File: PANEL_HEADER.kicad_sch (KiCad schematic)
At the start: 1 part, among them J4 Conn_01x02

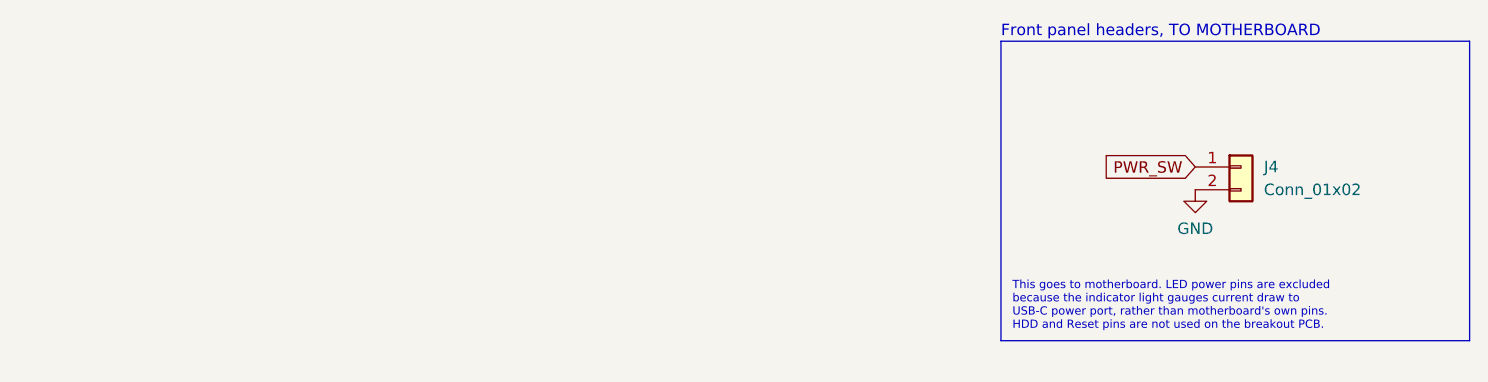
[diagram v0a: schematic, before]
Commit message: Mostly complete initial transfer to hierarchical schematic
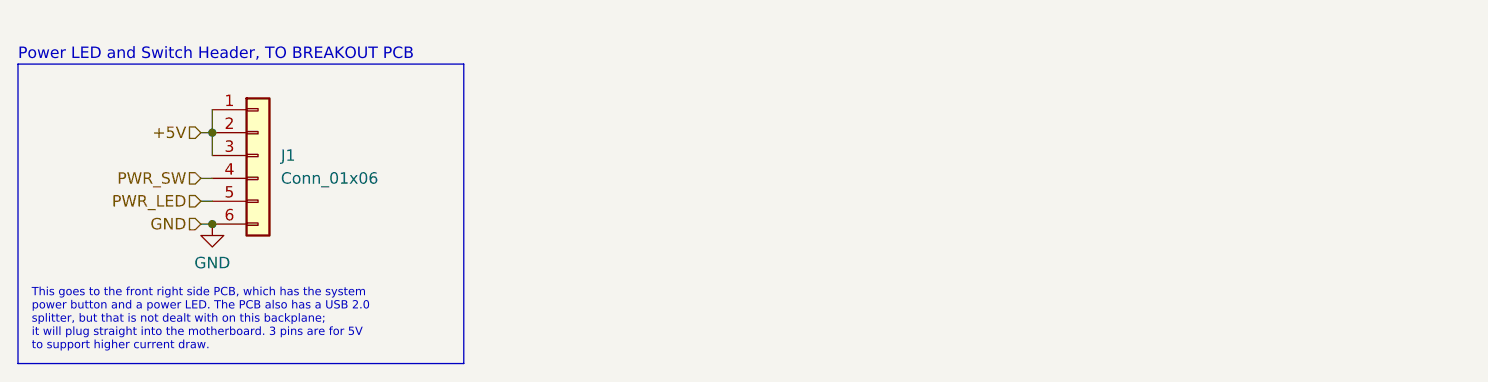
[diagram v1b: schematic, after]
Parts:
- removed J4: Conn_01x02, Connector_PinHeader_2.54mm:PinHeader_1x02_P2.54mm_Vertical_SMD_Pin1Left, symbol Connector_Generic:Conn_01x02
- added J1: Conn_01x06, Connector_PinSocket_2.54mm:PinSocket_1x06_P2.54mm_Horizontal, symbol Connector_Generic:Conn_01x06
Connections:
- net GND: now also J1.6 (Pin_6)
- net PWR_SW: now also J1.4 (Pin_4)
- new net +5V: J1.1 (Pin_1), J1.2 (Pin_2), J1.3 (Pin_3)
- new net PWR_LED: J1.5 (Pin_5)
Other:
- note added: "Power LED and Switch Header, TO BREAKOUT PCB"
- note added: "This goes to the front right side PCB, which has the system power button and a power LED. The PCB also has a USB 2.0 splitter, but that is not dealt with on this backplane; it will plug straight into the motherboard. 3 pins are for 5V to support higher current draw."
- note removed: "Front panel headers, TO MOTHERBOARD"
- note removed: "This goes to motherboard. LED power pins are excluded because the indicator light gauges current draw to USB-C power port, rather than motherboard's own pins. HDD and Reset pins are not used on the breakout PCB."
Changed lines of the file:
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@@
 	(paper "A5")
 	(rectangle
-		(start 133.35 20.32)
-		(end 185.42 53.594)
+		(start 24.13 22.86)
+		(end 73.66 56.134)
 		(stroke
 			(width 0)
@@
 		)
 	)
-	(text "Front panel headers, TO MOTHERBOARD"
-		(exclude_from_sim no)
-		(at 133.35 19.304 0)
-		(effects
-			(font
-				(size 1.27 1.27)
+	(text "This goes to the front right side PCB, which has the system \npower button and a power LED. The PCB also has a USB 2.0\nsplitter, but that is not dealt with on this backplane;\nit will plug straight into the motherboard. 3 pins are for 5V\nto support higher current draw."
+		(exclude_from_sim no)
+		(at 25.654 51.308 0)
+		(effects
+			(font
+				(size 0.9144 0.9144)
 			)
 			(justify left)
 		)
 	)
-	(text "This goes to motherboard. LED power pins are excluded\nbecause the indicator light gauges current draw to\nUSB-C power port, rather than motherboard's own pins.\nHDD and Reset pins are not used on the breakout PCB."
-		(exclude_from_sim no)
-		(at 134.62 49.784 0)
-		(effects
-			(font
-				(size 0.9144 0.9144)
+	(text "Power LED and Switch Header, TO BREAKOUT PCB"
+		(exclude_from_sim no)
+		(at 24.13 21.844 0)
+		(effects
+			(font
+				(size 1.27 1.27)
 			)
 			(justify left)
 		)
 	)
-	(global_label "PWR_SW"
-		(shape input)
-		(at 154.94 34.29 180)
-		(fields_autoplaced yes)
-		(effects
-			(font
-				(size 1.27 1.27)
-			)
-			(justify right)
-		)
-		(property "Intersheetrefs" "${INTERSHEET_REFS}"
-			(at 144.3349 34.29 0)
-			(hide yes)
-			(show_name no)
-			(do_not_autoplace no)
-			(effects
-				(font
-					(size 1.27 1.27)
-				)
-				(justify right)
-			)
+	(junction
+		(at 45.72 30.48)
+		(diameter 0)
+		(color 0 0 0 0)
+	)
+	(junction
+		(at 45.72 40.64)
+		(diameter 0)
+		(color 0 0 0 0)
+	)
+	(wire
+		(pts
+			(xy 44.45 35.56) (xy 45.72 35.56)
+		)
+		(stroke
+			(width 0)
+			(type default)
+		)
+	)
+	(wire
+		(pts
+			(xy 44.45 38.1) (xy 45.72 38.1)
+		)
+		(stroke
+			(width 0)
+			(type default)
+		)
+	)
+	(wire
+		(pts
+			(xy 45.72 27.94) (xy 45.72 30.48)
+		)
+		(stroke
+			(width 0)
+			(type default)
+		)
+	)
+	(wire
+		(pts
+			(xy 44.45 40.64) (xy 45.72 40.64)
+		)
+		(stroke
+			(width 0)
+			(type default)
+		)
+	)
+	(wire
+		(pts
+			(xy 45.72 30.48) (xy 45.72 33.02)
+		)
+		(stroke
+			(width 0)
+			(type default)
+		)
+	)
+	(wire
+		(pts
+			(xy 44.45 30.48) (xy 45.72 30.48)
+		)
+		(stroke
+			(width 0)
+			(type default)
+		)
+	)
+	(hierarchical_label "GND"
+		(shape input)
+		(at 44.45 40.64 180)
+		(effects
+			(font
+				(size 1.27 1.27)
+			)
+			(justify right)
+		)
+	)
+	(hierarchical_label "PWR_SW"
+		(shape input)
+		(at 44.45 35.56 180)
+		(effects
+			(font
+				(size 1.27 1.27)
+			)
+			(justify right)
+		)
+	)
+	(hierarchical_label "+5V"
+		(shape input)
+		(at 44.45 30.48 180)
+		(effects
+			(font
+				(size 1.27 1.27)
+			)
+			(justify right)
+		)
+	)
+	(hierarchical_label "PWR_LED"
+		(shape input)
+		(at 44.45 38.1 180)
+		(effects
+			(font
+				(size 1.27 1.27)
+			)
+			(justify right)
 		)
 	)
 	(symbol
-		(lib_id "power:GND")
-		(at 154.94 36.83 0)
-		(unit 1)
-		(body_style 1)
-		(exclude_from_sim no)
-		(in_bom yes)
-		(on_board yes)
-		(in_pos_files yes)
-		(dnp no)
-		(property "Reference" "#PWR0143"
-			(at 154.94 43.18 0)
-			(hide yes)
-			(show_name no)
-			(do_not_autoplace no)
-			(effects
-				(font
-					(size 1.27 1.27)
-				)
-			)
-		)
-		(property "Value" "GND"
-			(at 154.94 41.148 0)
-			(show_name no)
-			(do_not_autoplace no)
-			(effects
-				(font
-					(size 1.27 1.27)
-				)
-			)
-		)
-		(property "Footprint" ""
-			(at 154.94 36.83 0)
-			(hide yes)
-			(show_name no)
-			(do_not_autoplace no)
-			(effects
-				(font
-					(size 1.27 1.27)
-				)
-			)
-		)
-		(property "Datasheet" ""
-			(at 154.94 36.83 0)
-			(hide yes)
-			(show_name no)
-			(do_not_autoplace no)
-			(effects
-				(font
-					(size 1.27 1.27)
-				)
-			)
-		)
-		(property "Description" "Power symbol creates a global label with name \"GND\" , ground"
-			(at 154.94 36.83 0)
-			(hide yes)
-			(show_name no)
-			(do_not_autoplace no)
-			(effects
-				(font
-					(size 1.27 1.27)
-				)
-			)
-		)
-		(pin "1"
-		)
-		(instances
-			(project "other_connectors"
-				(path "/9b94df28-2798-4b39-aed9-30882f1bc4a5"
-					(reference "#PWR0143")
-					(unit 1)
-				)
-			)
-			(project "serverv2_backplane"
-				(path "/a6fda882-b5b2-43b7-bcc8-365357a6eb10"
-					(reference "#PWR0143")
-					(unit 1)
-				)
-			)
-		)
-	)
-	(symbol
-		(lib_id "Connector_Generic:Conn_01x02")
-		(at 160.02 34.29 0)
+		(lib_id "Connector_Generic:Conn_01x06")
+		(at 50.8 33.02 0)
 		(unit 1)
 		(body_style 1)
@@
 		(dnp no)
 		(fields_autoplaced yes)
-		(property "Reference" "J4"
-			(at 162.56 34.2899 0)
+		(property "Reference" "J1"
+			(at 53.34 33.0199 0)
 			(show_name no)
 			(do_not_autoplace no)
@@
 			)
 		)
-		(property "Value" "Conn_01x02"
-			(at 162.56 36.8299 0)
+		(property "Value" "Conn_01x06"
+			(at 53.34 35.5599 0)
 			(show_name no)
 			(do_not_autoplace no)
@@
 			)
 		)
-		(property "Footprint" "Connector_PinHeader_2.54mm:PinHeader_1x02_P2.54mm_Vertical_SMD_Pin1Left"
-			(at 160.02 34.29 0)
+		(property "Footprint" "Connector_PinSocket_2.54mm:PinSocket_1x06_P2.54mm_Horizontal"
+			(at 50.8 33.02 0)
 			(hide yes)
 			(show_name no)
@@
 		)
 		(property "Datasheet" ""
-			(at 160.02 34.29 0)
-			(hide yes)
-			(show_name no)
-			(do_not_autoplace no)
-			(effects
-				(font
-					(size 1.27 1.27)
-				)
-			)
-		)
-		(property "Description" "Generic connector, single row, 01x02, script generated (kicad-library-utils/schlib/autogen/connector/)"
-			(at 160.02 34.29 0)
-			(hide yes)
-			(show_name no)
-			(do_not_autoplace no)
-			(effects
-				(font
-					(size 1.27 1.27)
-				)
-			)
+			(at 50.8 33.02 0)
+			(hide yes)
+			(show_name no)
+			(do_not_autoplace no)
+			(effects
+				(font
+					(size 1.27 1.27)
+				)
+			)
+		)
+		(property "Description" "Generic connector, single row, 01x06, script generated (kicad-library-utils/schlib/autogen/connector/)"
+			(at 50.8 33.02 0)
+			(hide yes)
+			(show_name no)
+			(do_not_autoplace no)
+			(effects
+				(font
+					(size 1.27 1.27)
+				)
+			)
+		)
+		(pin "5"
+		)
+		(pin "6"
+		)
+		(pin "3"
+		)
+		(pin "2"
+		)
+		(pin "4"
 		)
 		(pin "1"
 		)
-		(pin "2"
-		)
 		(instances
-			(project "other_connectors"
-				(path "/9b94df28-2798-4b39-aed9-30882f1bc4a5"
-					(reference "J4")
+			(project "serverv2_backplane"
+				(path "/d38d6818-cf53-410d-afa3-a75a85b7c05a/71081068-7510-455e-b0a7-58ba4dd83771"
+					(reference "J1")
 					(unit 1)
 				)
 			)
+		)
+	)
+	(symbol
+		(lib_id "power:GND")
+		(at 45.72 40.64 0)
+		(unit 1)
+		(body_style 1)
+		(exclude_from_sim no)
+		(in_bom yes)
+		(on_board yes)
+		(in_pos_files yes)
+		(dnp no)
+		(property "Reference" "#PWR0142"
+			(at 45.72 46.99 0)
+			(hide yes)
+			(show_name no)
+			(do_not_autoplace no)
+			(effects
+				(font
+					(size 1.27 1.27)
+				)
+			)
+		)
+		(property "Value" "GND"
+			(at 45.72 44.958 0)
+			(show_name no)
+			(do_not_autoplace no)
+			(effects
+				(font
+					(size 1.27 1.27)
+				)
+			)
+		)
+		(property "Footprint" ""
+			(at 45.72 40.64 0)
+			(hide yes)
+			(show_name no)
+			(do_not_autoplace no)
+			(effects
+				(font
+					(size 1.27 1.27)
+				)
+			)
+		)
+		(property "Datasheet" ""
+			(at 45.72 40.64 0)
+			(hide yes)
+			(show_name no)
+			(do_not_autoplace no)
+			(effects
+				(font
+					(size 1.27 1.27)
+				)
+			)
+		)
+		(property "Description" "Power symbol creates a global label with name \"GND\" , ground"
+			(at 45.72 40.64 0)
+			(hide yes)
+			(show_name no)
+			(do_not_autoplace no)
+			(effects
+				(font
+					(size 1.27 1.27)
+				)
+			)
+		)
+		(pin "1"
+		)
+		(instances
 			(project "serverv2_backplane"
-				(path "/a6fda882-b5b2-43b7-bcc8-365357a6eb10"
-					(reference "J4")
+				(path "/d38d6818-cf53-410d-afa3-a75a85b7c05a/71081068-7510-455e-b0a7-58ba4dd83771"
+					(reference "#PWR0142")
 					(unit 1)
 				)
@@
 		)
 	)
-	(sheet_instances
-		(path "/"
-			(page "6")
-		)
-	)
-	(embedded_fonts no)
 )
